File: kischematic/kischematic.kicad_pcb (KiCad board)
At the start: 2 copper layers, 26.7 x 50 mm, 111 parts, among them IC1 BlueNRG, IC10 128x64OLED, IC2 EFM32ZG108, IC3 BQ297xx, IC4 AAT3672IWO-4.2-1, IC5 TPS6223xx, IC6 APDS-9303, IC7 APDS-9303, IC8 BSD840NH6327XTSA1, IC9 MMA8653FC, J1 Screw_Terminal_1x02, J2 Screw_Terminal_1x01, J3 Screw_Terminal_1x01, J4 0, J5 Screw_Terminal_1x01, J6 Screw_Terminal_1x01, J7 0, P1 CONN_01X01, P2 CONN_01X01, P3 CONN_01X01, P4 CONN_01X01, P5 CONN_01X01, P6 CONN_01X01, P7 CONN_01X01, P8 CONN_01X04, P9 CONN_01X04, SW1 SW_Push, SW2 SW_Push, U1 USB-C, U2 SWD_SPRING, U3 FT220X, Y1 32k, Y2 16M

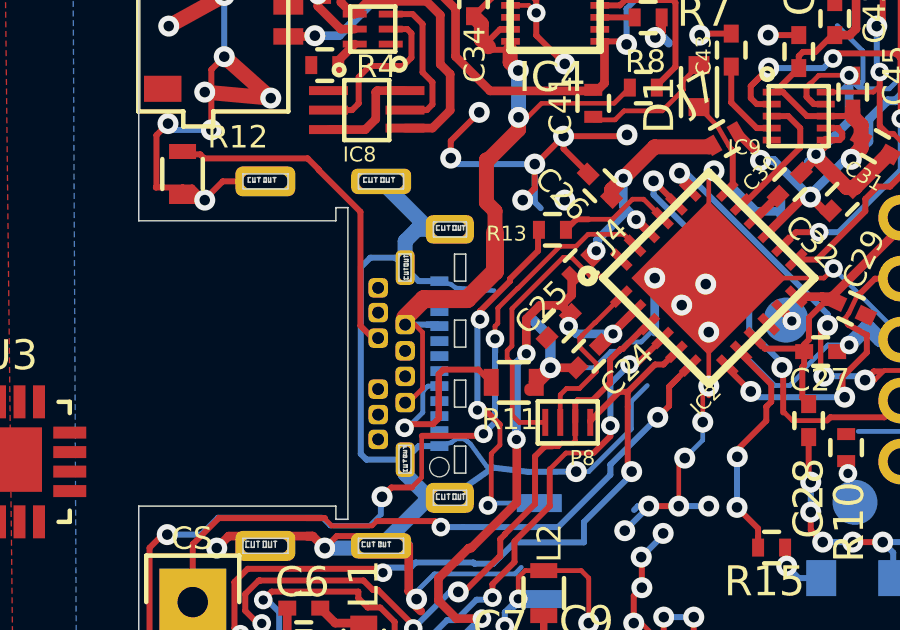
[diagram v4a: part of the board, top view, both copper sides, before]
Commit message: Remove more (hopefully) unnecessary USB connections.
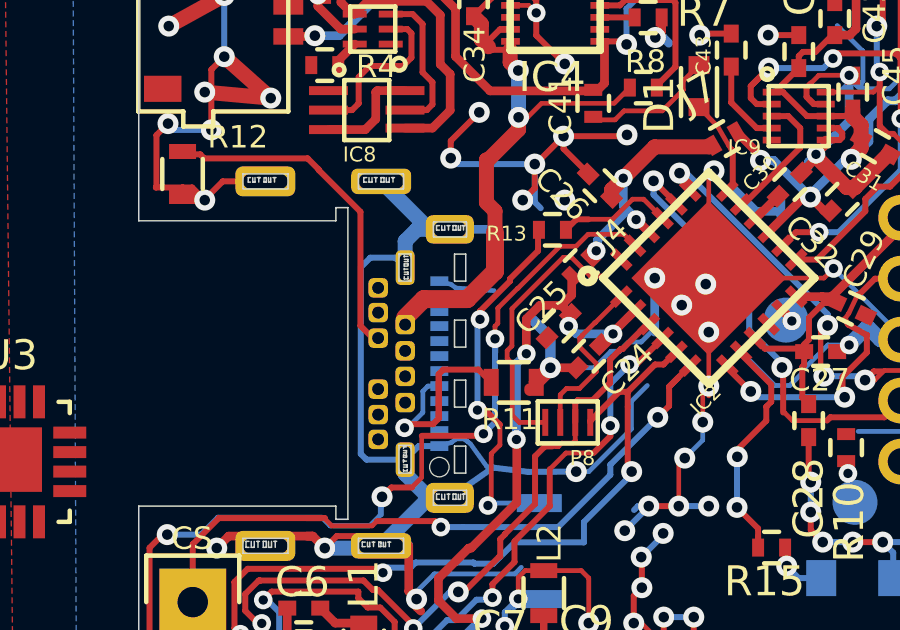
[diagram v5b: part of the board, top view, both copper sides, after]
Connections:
- U1 pad A9: VUSB -> Net-(U1-PadA9)
- U1 pad B9: VUSB -> Net-(U1-PadB9)
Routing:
- net VUSB: track 26.6 -> 21.4 mm
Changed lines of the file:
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@@
 (kicad_pcb (version 20160815) (host pcbnew "(2016-12-18 revision 3ffa37c)-master")
   (general
-    (links 259)
+    (links 257)
     (no_connects 8)
     (area 75.974999 24.974999 102.725001 75.025001)
     (thickness 1.6)
     (drawings 272)
-    (tracks 2033)
+    (tracks 2026)
     (zones 0)
     (modules 111)
-    (nets 127)
+    (nets 129)
   )
   (page A4)
@@
   (net 125 "Net-(U1-PadB6)")
   (net 126 "Net-(U1-PadB7)")
+  (net 127 "Net-(U1-PadA9)")
+  (net 128 "Net-(U1-PadB9)")
   (net_class Default "This is the default net class."
     (clearance 0.1525)
@@
     (add_net "Net-(U1-PadA7)")
     (add_net "Net-(U1-PadA8)")
+    (add_net "Net-(U1-PadA9)")
     (add_net "Net-(U1-PadB10)")
     (add_net "Net-(U1-PadB11)")
@@
     (add_net "Net-(U1-PadB7)")
     (add_net "Net-(U1-PadB8)")
+    (add_net "Net-(U1-PadB9)")
     (add_net "Net-(U3-Pad1)")
     (add_net "Net-(U3-Pad10)")
@@
     (pad "" np_thru_hole oval (at -3.2 0.69 90) (size 0.9 0.35) (drill oval 0.9 0.35) (layers *.Cu *.Mask))
     (pad B9 thru_hole roundrect (at -1.3 -1.14 90) (size 0.65 0.65) (drill 0.4) (layers *.Cu *.Mask)(roundrect_rratio 0.25)
-      (net 43 VUSB))
+      (net 128 "Net-(U1-PadB9)"))
     (pad B4 thru_hole roundrect (at 1.3 -1.14 90) (size 0.65 0.65) (drill 0.4) (layers *.Cu *.Mask)(roundrect_rratio 0.25)
       (net 43 VUSB))
@@
       (net 59 "Net-(U1-PadA10)"))
     (pad A9 smd rect (at 1.25 0 90) (size 0.3275 0.6) (layers B.Cu B.Paste B.Mask)
-      (net 43 VUSB))
+      (net 127 "Net-(U1-PadA9)"))
     (pad A8 smd rect (at 0.75 0 90) (size 0.3275 0.6) (layers B.Cu B.Paste B.Mask)
       (net 58 "Net-(U1-PadA8)"))
@@
   (segment (start 97.4 43.4) (end 97.4 43.925) (width 0.29) (layer B.Cu) (net 0))
   (segment (start 97.4 43.4) (end 97.4 43.75) (width 0.29) (layer B.Cu) (net 0))
+  (segment (start 86.37 44.375) (end 87.825 44.375) (width 0.29) (layer B.Cu) (net 1))
   (via (at 98.575 41.875) (size 0.62) (drill 0.31) (layers F.Cu B.Cu) (net 1))
   (segment (start 98.575 41.875) (end 98.325 42.125) (width 0.29) (layer B.Cu) (net 1))
@@
   (via (at 94 53.6) (size 0.7) (drill 0.35) (layers F.Cu B.Cu) (net 1))
   (segment (start 98.08 35.71) (end 98.08 34.91) (width 0.16) (layer F.Cu) (net 1))
-  (segment (start 86.02 46.1) (end 85.33 46.1) (width 0.2) (layer B.Cu) (net 1) (status 10))
-  (segment (start 85.33 46.1) (end 84.88 45.65) (width 0.2) (layer B.Cu) (net 1) (status 20))
   (via (at 88.2 57.6) (size 0.62) (drill 0.31) (layers F.Cu B.Cu) (net 1))
   (segment (start 79.6 54.6) (end 80 55) (width 0.2) (layer F.Cu) (net 1) (status 30))
@@
   (segment (start 91.845 40.175) (end 92.37 39.65) (width 0.16) (layer F.Cu) (net 43))
   (segment (start 89.425 40.175) (end 91.845 40.175) (width 0.1525) (layer F.Cu) (net 43))
-  (segment (start 85.6 47.55) (end 85.97 47.55) (width 0.2) (layer B.Cu) (net 43) (status 20))
   (segment (start 88.3925 36.11) (end 87.95 36.11) (width 0.2) (layer F.Cu) (net 43) (status 10))
   (segment (start 87.95 36.11) (end 87.78 36.28) (width 0.2) (layer F.Cu) (net 43))
@@
   (segment (start 87.42 37.53) (end 87.16 37.27) (width 0.5) (layer F.Cu) (net 43) (status 20))
   (segment (start 87.42 38.05) (end 87.66 38.29) (width 0.5) (layer F.Cu) (net 43))
-  (segment (start 85.46 47.81) (end 85.2 47.55) (width 0.16) (layer F.Cu) (net 43) (status 20))
-  (segment (start 85.46 49.68) (end 85.46 47.81) (width 0.16) (layer F.Cu) (net 43))
-  (segment (start 84.99 50.15) (end 85.46 49.68) (width 0.16) (layer F.Cu) (net 43) (status 10))
-  (segment (start 85.2 47.55) (end 84.88 47.55) (width 0.16) (layer F.Cu) (net 43) (status 30))
-  (segment (start 84.88 50.15) (end 84.99 50.15) (width 0.16) (layer F.Cu) (net 43) (status 30))
   (segment (start 87.66 38.29) (end 87.66 38.09) (width 0.2) (layer F.Cu) (net 43))
   (segment (start 87.66 38.09) (end 88.04 37.71) (width 0.2) (layer F.Cu) (net 43))
@@
   (segment (start 87.875 45.775) (end 87.875 44.475) (width 0.6) (layer F.Cu) (net 43))
   (segment (start 84.88 47.55) (end 84.88 47.32) (width 0.29) (layer F.Cu) (net 43) (status 30))
-  (segment (start 84.88 47.55) (end 85.97 47.55) (width 0.2) (layer B.Cu) (net 43) (status 30))
-  (segment (start 84.88 50.15) (end 85 50.15) (width 0.16) (layer B.Cu) (net 43) (status 30))
-  (segment (start 84.88 50.15) (end 84.95 50.15) (width 0.16) (layer B.Cu) (net 43) (status 30))
-  (segment (start 84.88 50.15) (end 85.05 50.15) (width 0.2) (layer B.Cu) (net 43) (status 30))
-  (segment (start 85.97 47.55) (end 86.02 47.6) (width 0.2) (layer B.Cu) (net 43) (status 30))
   (segment (start 88.3925 35.3375) (end 89.22 34.51) (width 0.2) (layer F.Cu) (net 45))
   (segment (start 89.22 34.51) (end 89.43 34.51) (width 0.2) (layer F.Cu) (net 45) (status 20))
@@
   (segment (start 84.88 48.425) (end 84.935 48.425) (width 0.16) (layer B.Cu) (net 125) (status 30))
   (segment (start 84.88 49.275) (end 84.835 49.275) (width 0.16) (layer B.Cu) (net 126) (status 30))
+  (segment (start 85.97 47.55) (end 86.02 47.6) (width 0.2) (layer B.Cu) (net 127) (status 30))
+  (segment (start 84.88 50.15) (end 84.99 50.15) (width 0.16) (layer F.Cu) (net 128) (status 30))
+  (segment (start 84.88 50.15) (end 85 50.15) (width 0.16) (layer B.Cu) (net 128) (status 30))
+  (segment (start 84.88 50.15) (end 84.95 50.15) (width 0.16) (layer B.Cu) (net 128) (status 30))
+  (segment (start 84.88 50.15) (end 85.05 50.15) (width 0.2) (layer B.Cu) (net 128) (status 30))
   (zone (net 1) (net_name GND) (layer F.Cu) (hatch edge 0.508)
     (connect_pads (clearance 0.18))

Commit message: More USB work.
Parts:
- added U4: FT200XD, Housings_DFN_QFN:DFN-10-1EP_3x3mm_Pitch0.5mm, F.Cu at (73.7, 35.1)
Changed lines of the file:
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@@
 (kicad_pcb (version 20160815) (host pcbnew "(2016-12-18 revision 3ffa37c)-master")
   (general
-    (links 257)
-    (no_connects 8)
+    (links 260)
+    (no_connects 11)
     (area 75.974999 24.974999 102.725001 75.025001)
     (thickness 1.6)
@@
     (tracks 2026)
     (zones 0)
-    (modules 111)
-    (nets 129)
+    (modules 112)
+    (nets 140)
   )
   (page A4)
@@
   (net 127 "Net-(U1-PadA9)")
   (net 128 "Net-(U1-PadB9)")
+  (net 129 "Net-(U4-Pad11)")
+  (net 130 "Net-(U4-Pad10)")
+  (net 131 "Net-(U4-Pad9)")
+  (net 132 "Net-(U4-Pad8)")
+  (net 133 "Net-(U4-Pad7)")
+  (net 134 "Net-(U4-Pad6)")
+  (net 135 "Net-(U4-Pad5)")
+  (net 136 "Net-(U4-Pad4)")
+  (net 137 "Net-(U4-Pad3)")
+  (net 138 "Net-(U4-Pad2)")
+  (net 139 "Net-(U4-Pad1)")
   (net_class Default "This is the default net class."
     (clearance 0.1525)
@@
     (add_net "Net-(U3-Pad8)")
     (add_net "Net-(U3-Pad9)")
+    (add_net "Net-(U4-Pad1)")
+    (add_net "Net-(U4-Pad10)")
+    (add_net "Net-(U4-Pad11)")
+    (add_net "Net-(U4-Pad2)")
+    (add_net "Net-(U4-Pad3)")
+    (add_net "Net-(U4-Pad4)")
+    (add_net "Net-(U4-Pad5)")
+    (add_net "Net-(U4-Pad6)")
+    (add_net "Net-(U4-Pad7)")
+    (add_net "Net-(U4-Pad8)")
+    (add_net "Net-(U4-Pad9)")
     (add_net PIEZO)
     (add_net PIEZOGND)
@@
     (add_net VUSB)
   )
+  (module Housings_DFN_QFN:DFN-10-1EP_3x3mm_Pitch0.5mm (layer F.Cu)
+    (at 73.7 35.15)
+    (descr "10-Lead Plastic Dual Flat, No Lead Package (MF) - 3x3x0.9 mm Body [DFN] (see Microchip Packaging Specification 00000049BS.pdf)")
+    (tags "DFN 0.5")
+    (attr smd)
+    (fp_text reference U4 (at 0 -2.575) (layer F.SilkS)
+      (effects (font (size 1 1) (thickness 0.15)))
+    )
+    (fp_text value FT200XD (at 0 2.575) (layer F.Fab)
+      (effects (font (size 1 1) (thickness 0.15)))
+    )
+    (fp_line (start -1.95 -1.65) (end 1.225 -1.65) (layer F.SilkS) (width 0.15))
+    (fp_line (start -1.225 1.65) (end 1.225 1.65) (layer F.SilkS) (width 0.15))
+    (fp_line (start -2.15 1.85) (end 2.15 1.85) (layer F.CrtYd) (width 0.05))
+    (fp_line (start -2.15 -1.85) (end 2.15 -1.85) (layer F.CrtYd) (width 0.05))
+    (fp_line (start 2.15 -1.85) (end 2.15 1.85) (layer F.CrtYd) (width 0.05))
+    (fp_line (start -2.15 -1.85) (end -2.15 1.85) (layer F.CrtYd) (width 0.05))
+    (fp_line (start -1.5 -0.5) (end -0.5 -1.5) (layer F.Fab) (width 0.15))
+    (fp_line (start -1.5 1.5) (end -1.5 -0.5) (layer F.Fab) (width 0.15))
+    (fp_line (start 1.5 1.5) (end -1.5 1.5) (layer F.Fab) (width 0.15))
+    (fp_line (start 1.5 -1.5) (end 1.5 1.5) (layer F.Fab) (width 0.15))
+    (fp_line (start -0.5 -1.5) (end 1.5 -1.5) (layer F.Fab) (width 0.15))
+    (pad 11 smd rect (at -0.3875 -0.62) (size 0.775 1.24) (layers F.Cu F.Paste F.Mask)
+      (net 129 "Net-(U4-Pad11)") (solder_paste_margin_ratio -0.2))
+    (pad 11 smd rect (at -0.3875 0.62) (size 0.775 1.24) (layers F.Cu F.Paste F.Mask)
+      (net 129 "Net-(U4-Pad11)") (solder_paste_margin_ratio -0.2))
+    (pad 11 smd rect (at 0.3875 -0.62) (size 0.775 1.24) (layers F.Cu F.Paste F.Mask)
+      (net 129 "Net-(U4-Pad11)") (solder_paste_margin_ratio -0.2))
+    (pad 11 smd rect (at 0.3875 0.62) (size 0.775 1.24) (layers F.Cu F.Paste F.Mask)
+      (net 129 "Net-(U4-Pad11)") (solder_paste_margin_ratio -0.2))
+    (pad 10 smd rect (at 1.55 -1) (size 0.65 0.3) (layers F.Cu F.Paste F.Mask)
+      (net 130 "Net-(U4-Pad10)"))
+    (pad 9 smd rect (at 1.55 -0.5) (size 0.65 0.3) (layers F.Cu F.Paste F.Mask)
+      (net 131 "Net-(U4-Pad9)"))
+    (pad 8 smd rect (at 1.55 0) (size 0.65 0.3) (layers F.Cu F.Paste F.Mask)
+      (net 132 "Net-(U4-Pad8)"))
+    (pad 7 smd rect (at 1.55 0.5) (size 0.65 0.3) (layers F.Cu F.Paste F.Mask)
+      (net 133 "Net-(U4-Pad7)"))
+    (pad 6 smd rect (at 1.55 1) (size 0.65 0.3) (layers F.Cu F.Paste F.Mask)
+      (net 134 "Net-(U4-Pad6)"))
+    (pad 5 smd rect (at -1.55 1) (size 0.65 0.3) (layers F.Cu F.Paste F.Mask)
+      (net 135 "Net-(U4-Pad5)"))
+    (pad 4 smd rect (at -1.55 0.5) (size 0.65 0.3) (layers F.Cu F.Paste F.Mask)
+      (net 136 "Net-(U4-Pad4)"))
+    (pad 3 smd rect (at -1.55 0) (size 0.65 0.3) (layers F.Cu F.Paste F.Mask)
+      (net 137 "Net-(U4-Pad3)"))
+    (pad 2 smd rect (at -1.55 -0.5) (size 0.65 0.3) (layers F.Cu F.Paste F.Mask)
+      (net 138 "Net-(U4-Pad2)"))
+    (pad 1 smd rect (at -1.55 -1) (size 0.65 0.3) (layers F.Cu F.Paste F.Mask)
+      (net 139 "Net-(U4-Pad1)"))
+    (model Housings_DFN_QFN.3dshapes/DFN-10-1EP_3x3mm_Pitch0.5mm.wrl
+      (at (xyz 0 0 0))
+      (scale (xyz 1 1 1))
+      (rotate (xyz 0 0 0))
+    )
+  )
   (module newlightmeter:QFN_16 (layer F.Cu)

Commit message: Minor.
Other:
- board text added: "PIEZO"
- board text added: "PIEZOG"
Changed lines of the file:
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@@
     (area 75.974999 24.974999 102.725001 75.025001)
     (thickness 1.6)
-    (drawings 272)
+    (drawings 274)
     (tracks 2026)
     (zones 0)
@@
   (module newlightmeter:SMALLWIREPAD (layer B.Cu)
     (at 97.575 47.4)
-    (fp_text reference TP1 (at -0.05 1.25) (layer B.SilkS)
+    (fp_text reference TP1 (at -0.05 1.25) (layer B.SilkS) hide
       (effects (font (size 0.5 0.5) (thickness 0.125)) (justify mirror))
     )
@@
   (module newlightmeter:SMALLWIREPAD (layer B.Cu)
     (at 99.875 53.475)
-    (fp_text reference TP2 (at 0 1.2) (layer B.SilkS)
+    (fp_text reference TP2 (at 0 1.2) (layer B.SilkS) hide
       (effects (font (size 0.5 0.5) (thickness 0.125)) (justify mirror))
     )
@@
       (net 7 "Net-(C7-Pad2)"))
   )
+  (gr_text "PIEZOG\n" (at 100 54.725) (layer B.SilkS)
+    (effects (font (size 0.75 0.75) (thickness 0.1875)) (justify mirror))
+  )
+  (gr_text "PIEZO\n" (at 97.6 48.75) (layer B.SilkS)
+    (effects (font (size 0.75 0.75) (thickness 0.1875)) (justify mirror))
+  )
   (gr_line (start 86.66 52) (end 86.81 52) (layer Eco2.User) (width 0.05))

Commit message: Before routing attempt.
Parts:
- removed J1: Screw_Terminal_1x02, newlightmeter:503763-0291
- removed U3: FT220X, newlightmeter:QFN_16
- added TP3: TEST, newlightmeter:SMALLWIREPAD, F.Cu at (80.8, 35.2)
- added TP4: TEST, newlightmeter:SMALLWIREPAD, F.Cu at (82.8, 34.0)
- moved U4 5.59 mm to (78.6, 37.9), turned to 90 degrees
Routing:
- net GND: track 472.5 -> 451.7 mm, vias 165 -> 159
- net BAT+: track 29.3 -> 31.6 mm
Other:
- board text added: "BAT+"
- board text added: "BAT-"
